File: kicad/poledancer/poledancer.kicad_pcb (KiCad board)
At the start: 4 copper layers, 80 x 80 mm, 166 parts, among them J1 Conn_01x01, J2 Conn_01x02, J3 Conn_02x20_Odd_Even, Q1 MMBT3904, U1 TL074, U10 TL074, U11 PS508, U12 M24C02-WMN, U13 PCA9555D, U14 AD5328, U2 SSI2190, U3 AS3364, U4 TL074, U5 SSI2140, U6 AD5328, U7 DG442xY, U8 LM4040AIM3-2.5, U9 PS508

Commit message: minor tweaks, thinking it's about done
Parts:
- moved R46 1.02 mm to (90.4, 47.2)
- moved R31 0.85 mm to (85.4, 49.4)
- moved R26 0.57 mm to (83.8, 46.2)
- moved R20 0.57 mm to (83.8, 42.6)
- moved R21 0.57 mm to (83.8, 39.0)
- moved R24 0.40 mm to (86.1, 46.2)
- moved R3 0.40 mm to (83.8, 35.0)
- moved R19 0.40 mm to (86.1, 42.6)
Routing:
- net GND: track 358.1 -> 354.6 mm, vias 103 -> 108
- net /filter_ssi2140/POLE3_BUFFERED: track 77.5 -> 75.8 mm
- net /filter_ssi2140/POLE4_BUFFERED: track 72.8 -> 71.5 mm
- net /filter_ssi2140/POLE2_BUFFERED: track 72.9 -> 71.7 mm
- net /filter_ssi2140/P2_OUT: track 18.1 -> 19.2 mm
- net Net-(U5C-IN3): track 16.7 -> 17.4 mm
- net /QCTRL_CURRENT: track 45.7 -> 45.0 mm
- net /filter_ssi2140/POLE1_BUFFERED: track 62.7 -> 62.0 mm
- net Net-(U2F-IN6-): track 8.87 -> 9.51 mm
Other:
- board text added: "IN1: CARD A1 CARD A2 CARD B2 CARD C1 CARD D2 CARD E1 CARD F2 CARD G1"
- board text added: "IN2: CARD A1 CARD A2 CARD B1 CARD B2 CARD C2 CARD D1 CARD E2 CARD F1"

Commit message: v0.1 sent to manufacture
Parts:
- U2: footprint Package_SO:SSOP-24_3.9x8.7mm_P0.635mm -> project_footprints:SSOP-24_3.9x8.7mm_P0.635mm_HandSolder
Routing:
- net +12V: track 208.4 -> 207.7 mm
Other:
- board text added: "JLCJLCJLCJLC"

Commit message: fix label error between pole2/pole4 in DAC channels in schematic.  no layout change.
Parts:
- C10: value 22n -> 0.1u
- C22, C25, C27, C6, C7: value 22n -> 47n
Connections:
- R13 pad 2: /dac_2190/POLE2_CTRL -> /dac_2190/POLE4_CTRL
- R48 pad 2: /dac_2190/POLE4_CTRL -> /dac_2190/POLE2_CTRL
- U6 pad 5: /dac_2190/POLE2_CTRL -> /dac_2190/POLE4_CTRL
- U6 pad 6: /dac_2190/POLE4_CTRL -> /dac_2190/POLE2_CTRL
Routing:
- net /dac_2190/POLE4_CTRL: track 2.29 -> 7.48 mm
- net /dac_2190/POLE2_CTRL: track 7.48 -> 2.29 mm

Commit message: updates to z3340 and poledancer schematics and layout
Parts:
- C30: value 150p -> 22p
- R13, R16, R48, R50, R51: value 10k -> 6k2
- R14, R17, R53, R55, R57: value 15k -> 6k2
- R18, R61: value 47k -> 20k
- R4: value 47k -> 100k
- R52: value 4k7 -> 3k
- R66: value 39k -> 150k
- R69: value 27k -> 24k
- U2: footprint project_footprints:SSOP-24_3.9x8.7mm_P0.635mm_HandSolder -> Package_SO:SSOP-24_3.9x8.7mm_P0.635mm
- U5: footprint project_footprints:SSOP-20_3.9x8.7mm_P0.635mm_HandSolder -> Package_SO:SSOP-20_4.4x6.5mm_P0.65mm
- moved R4 35.0 mm to (104.0, 55.8)
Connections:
- R4 pad 2: Net-(U2F-CTRL6) -> Net-(U4D--)
- U2 pad 20: Net-(U2F-CTRL6) -> unconnected-(U2F-CTRL6-Pad20)
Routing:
- net Net-(U2F-CTRL6): track 7.46 -> 0.00 mm
- net Net-(U4D--): track 39.9 -> 42.7 mm
- net GND: track 355.0 -> 355.7 mm
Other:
- board text added: "OFFSET"
- board text added: "POLE DANCER V0.1 2/2025"
- board text added: "SCALING"
- board text removed: "POLE DANCER V0.1 12/2024"

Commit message: Release ready files for Pole Dancer v0.2
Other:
- board text added: "POLE DANCER V0.2 2/2025"
- board text added: "SCALE"
- board text removed: "POLE DANCER V0.1 2/2025"
- board text removed: "SCALING"
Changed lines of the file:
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@@
   (title_block
     (title "Zoxnoxious Pole Dancer Mixing Filter")
-    (date "2024-11-17")
-    (rev "0.1")
+    (date "2025-02-13")
+    (rev "0.2")
     (company "Zoxnoxious Engineering")
   )
@@
     (effects (font (size 1 1) (thickness 0.15)))
   )
-  (gr_text "SCALING" (at 114.2 63.6 90) (layer "F.SilkS")
+  (gr_text "SCALE" (at 114.2 62.6 90) (layer "F.SilkS")
     (effects (font (size 0.8 0.8) (thickness 0.09)) (justify left bottom))
   )
-  (gr_text "POLE DANCER V0.1 2/2025" (at 143.4 57.4 90) (layer "F.SilkS")
+  (gr_text "POLE DANCER V0.2 2/2025" (at 143.4 57.4 90) (layer "F.SilkS")
     (effects (font (size 1 1) (thickness 0.15)))
   )

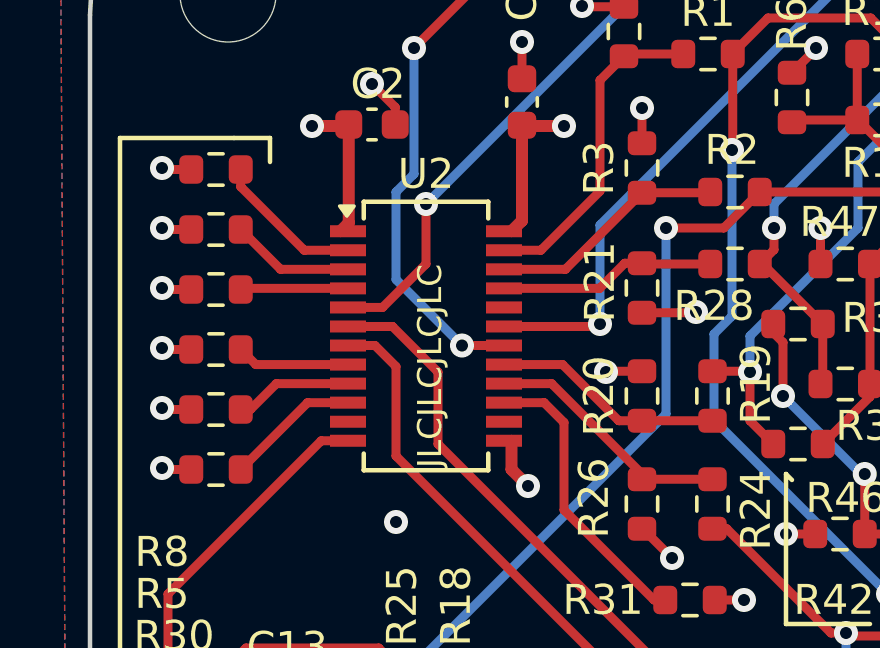
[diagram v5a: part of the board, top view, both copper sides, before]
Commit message: updated gerber files for pole dancer and updated tooling holes for all designs
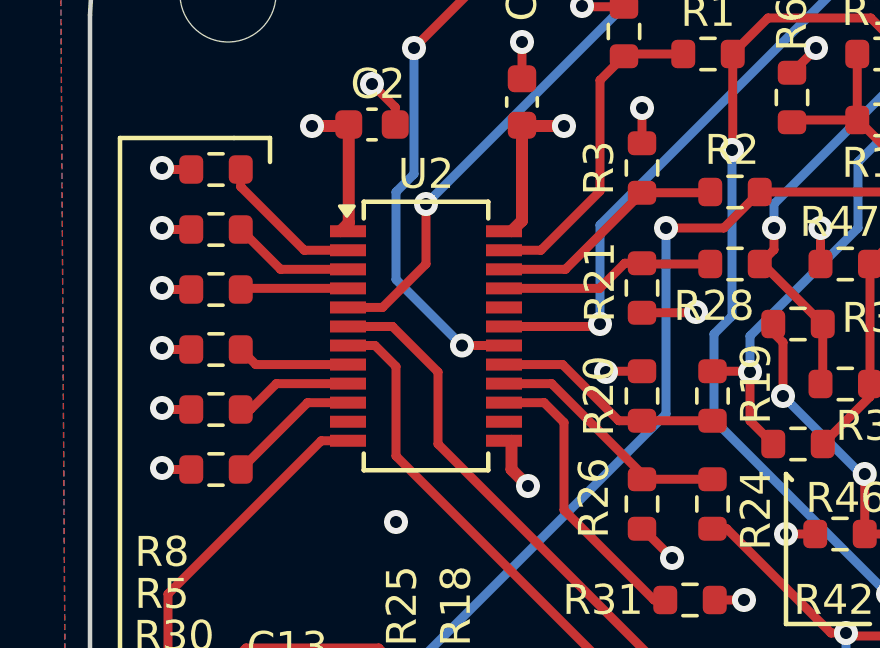
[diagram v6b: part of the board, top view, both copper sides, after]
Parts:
- added G***: LOGO, project_footprints:poledancer_logo, B.Cu at (119.0, 56.4)
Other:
- board text removed: "JLCJLCJLCJLC"
